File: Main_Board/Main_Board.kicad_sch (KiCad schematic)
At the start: 0 parts

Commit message: PCB init
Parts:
- added H1, H2: MountingHole_Pad, MountingHole:MountingHole_3.2mm_M3_DIN965_Pad_TopBottom, symbol Mechanical:MountingHole_Pad
- added H3, H4: MountingHole_Pad, MountingHole:MountingHole_2.2mm_M2, symbol Mechanical:MountingHole_Pad
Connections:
- new net GND: H1.1, H2.1, H3.1, H4.1

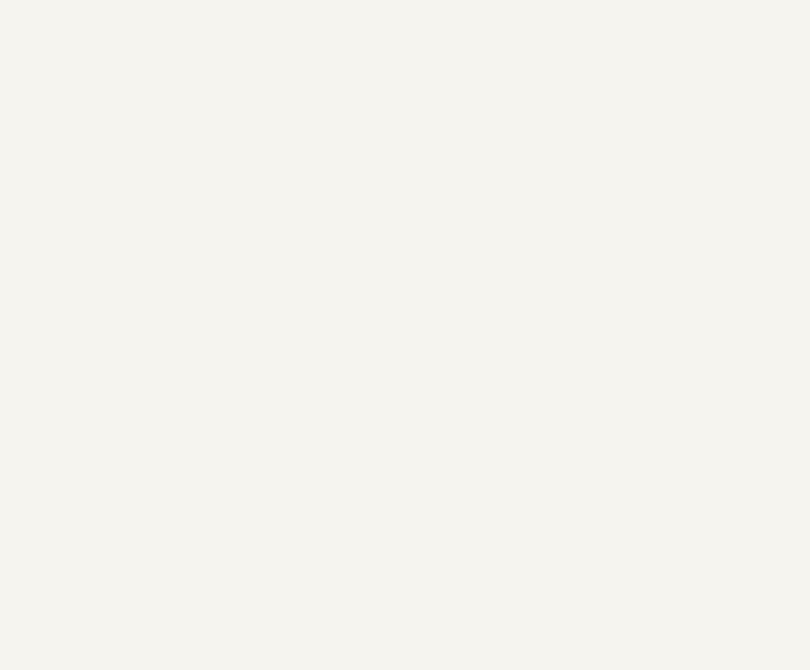
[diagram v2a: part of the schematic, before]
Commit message: Add pyro channels x2
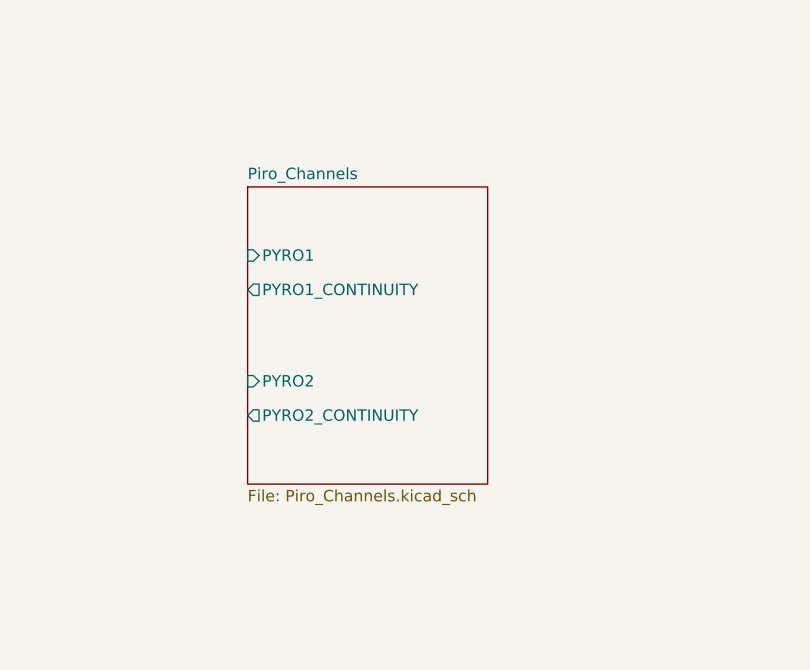
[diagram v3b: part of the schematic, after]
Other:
- added sheet Piro_Channels (Piro_Channels.kicad_sch)
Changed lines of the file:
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@@
 		(dnp no)
 		(fields_autoplaced yes)
-		(property "Reference" "#PWR096"
+		(property "Reference" "#PWR04"
 			(at 58.42 38.1 0)
 			(hide yes)
@@
 			(project "Main_Board"
 				(path "/7481738f-7c20-40bb-99b0-6ccd4168db33"
-					(reference "#PWR096")
+					(reference "#PWR04")
 					(unit 1)
 				)
@@
 		(dnp no)
 		(fields_autoplaced yes)
-		(property "Reference" "#PWR093"
+		(property "Reference" "#PWR01"
 			(at 31.75 38.1 0)
 			(hide yes)
@@
 			(project "Main_Board"
 				(path "/7481738f-7c20-40bb-99b0-6ccd4168db33"
-					(reference "#PWR093")
+					(reference "#PWR01")
 					(unit 1)
 				)
@@
 		(dnp no)
 		(fields_autoplaced yes)
-		(property "Reference" "#PWR094"
+		(property "Reference" "#PWR02"
 			(at 40.64 38.1 0)
 			(hide yes)
@@
 			(project "Main_Board"
 				(path "/7481738f-7c20-40bb-99b0-6ccd4168db33"
-					(reference "#PWR094")
+					(reference "#PWR02")
 					(unit 1)
 				)
@@
 		(dnp no)
 		(fields_autoplaced yes)
-		(property "Reference" "#PWR095"
+		(property "Reference" "#PWR03"
 			(at 49.53 38.1 0)
 			(hide yes)
@@
 			(project "Main_Board"
 				(path "/7481738f-7c20-40bb-99b0-6ccd4168db33"
-					(reference "#PWR095")
+					(reference "#PWR03")
 					(unit 1)
 				)
@@
 				)
 			)
+		)
+	)
+	(sheet
+		(at 93.98 78.74)
+		(size 26.67 33.02)
+		(exclude_from_sim no)
+		(in_bom yes)
+		(on_board yes)
+		(dnp no)
+		(fields_autoplaced yes)
+		(stroke
+			(width 0.1524)
+			(type solid)
+		)
+		(fill
+			(color 0 0 0 0)
+		)
+		(property "Sheetname" "Piro_Channels"
+			(at 93.98 78.0284 0)
+			(show_name no)
+			(do_not_autoplace no)
+			(effects
+				(font
+					(size 1.27 1.27)
+				)
+				(justify left bottom)
+			)
+		)
+		(property "Sheetfile" "Piro_Channels.kicad_sch"
+			(at 93.98 112.3446 0)
+			(show_name no)
+			(do_not_autoplace no)
+			(effects
+				(font
+					(size 1.27 1.27)
+				)
+				(justify left top)
+			)
+		)
+		(pin "PYRO2_CONTINUITY" output
+			(at 93.98 104.14 180)
+			(effects
+				(font
+					(size 1.27 1.27)
+				)
+				(justify left)
+			)
+		)
+		(pin "PYRO2" input
+			(at 93.98 100.33 180)
+			(effects
+				(font
+					(size 1.27 1.27)
+				)
+				(justify left)
+			)
+		)
+		(pin "PYRO1_CONTINUITY" output
+			(at 93.98 90.17 180)
+			(effects
+				(font
+					(size 1.27 1.27)
+				)
+				(justify left)
+			)
+		)
+		(pin "PYRO1" input
+			(at 93.98 86.36 180)
+			(effects
+				(font
+					(size 1.27 1.27)
+				)
+				(justify left)
+			)
+		)
+		(instances
+			(project "Main_Board"
+				(path "/7481738f-7c20-40bb-99b0-6ccd4168db33"
+					(page "10")
+				)
+			)

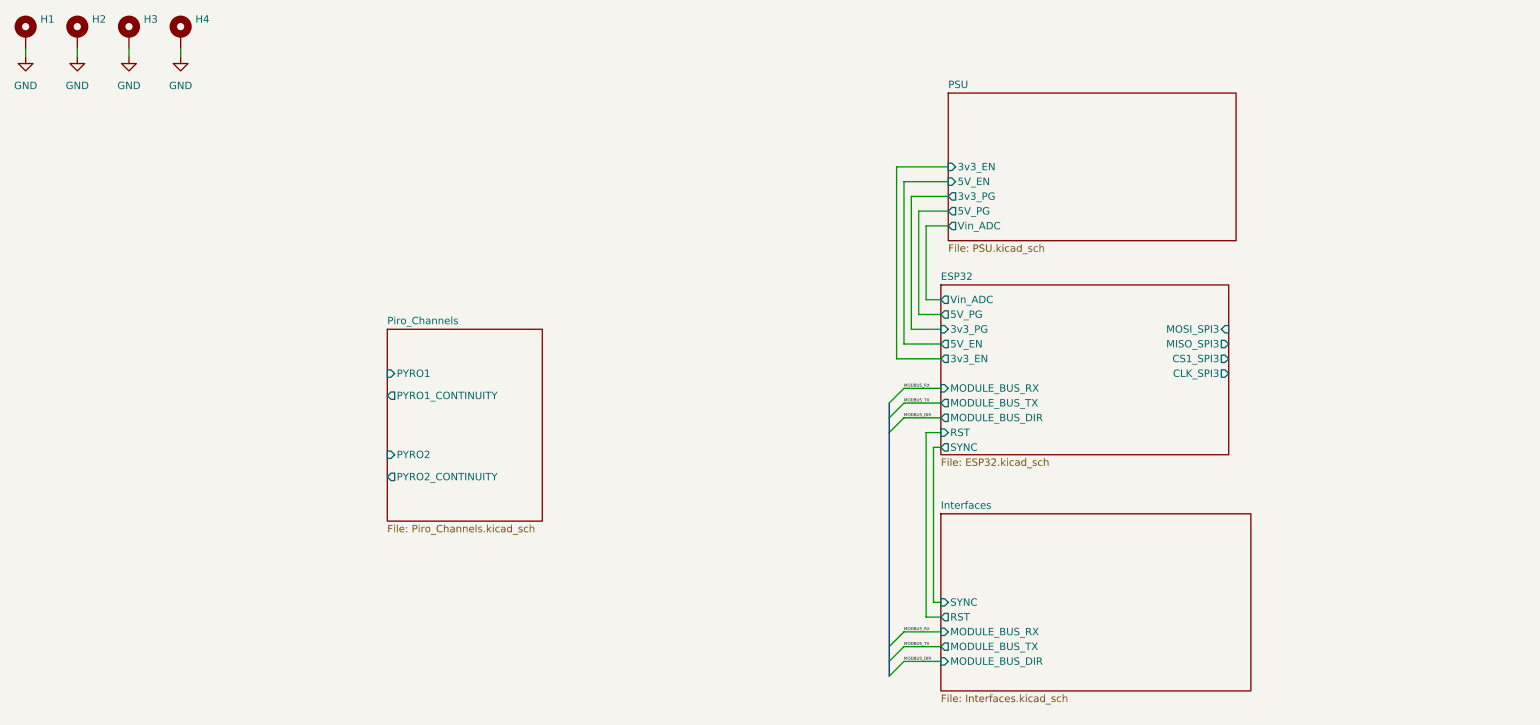
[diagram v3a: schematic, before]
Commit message: Module bus fix
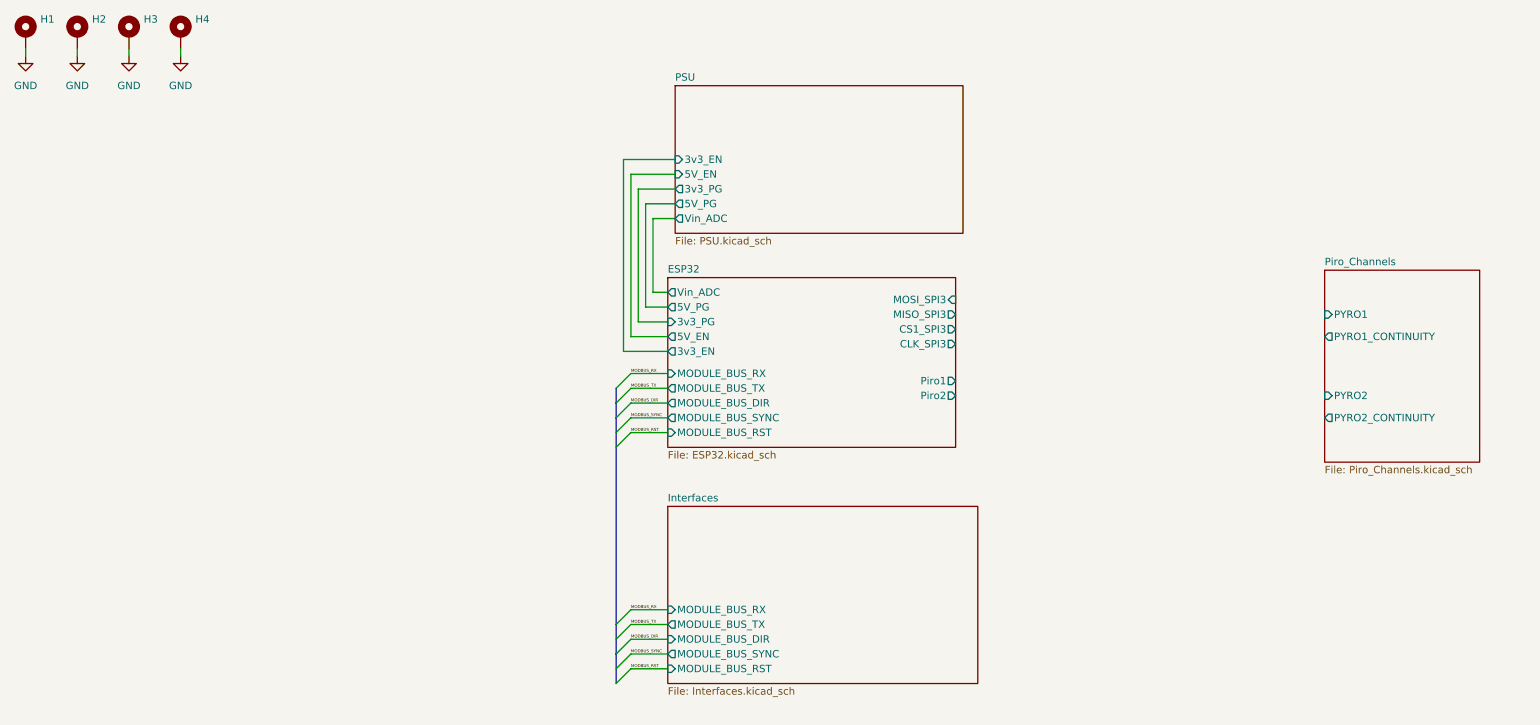
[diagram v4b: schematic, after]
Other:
- sheet ESP32 ports: added MODULE_BUS_RST, MODULE_BUS_SYNC, Piro1, Piro2; removed RST, SYNC
- sheet Interfaces ports: added MODULE_BUS_RST, MODULE_BUS_SYNC; removed RST, SYNC

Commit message: Update main sheet for pyros
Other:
- sheet ESP32 ports: added PYRO1, PYRO1_CONTINUITY, PYRO2, PYRO2_CONTINUITY; removed Piro1, Piro2
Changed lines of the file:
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@@
+	(wire
+		(pts
+			(xy 191.77 92.71) (xy 207.01 92.71)
+		)
+		(stroke
+			(width 0)
+			(type default)
+		)
+	)
 	(wire
 		(pts
@@
 	(wire
 		(pts
+			(xy 191.77 87.63) (xy 207.01 87.63)
+		)
+		(stroke
+			(width 0)
+			(type default)
+		)
+	)
+	(wire
+		(pts
 			(xy 135.89 52.07) (xy 135.89 80.01)
 		)
@@
 	(wire
 		(pts
+			(xy 191.77 90.17) (xy 207.01 90.17)
+		)
+		(stroke
+			(width 0)
+			(type default)
+		)
+	)
+	(wire
+		(pts
 			(xy 142.24 74.93) (xy 138.43 74.93)
 		)
@@
 		(pts
 			(xy 133.35 91.44) (xy 133.35 93.98)
+		)
+		(stroke
+			(width 0)
+			(type default)
+		)
+	)
+	(wire
+		(pts
+			(xy 191.77 95.25) (xy 207.01 95.25)
 		)
 		(stroke
@@
 	)
 	(sheet
-		(at 255.27 68.58)
-		(size 26.67 33.02)
+		(at 207.01 83.82)
+		(size 26.67 15.24)
 		(exclude_from_sim no)
 		(in_bom yes)
@@
 		)
 		(property "Sheetname" "Piro_Channels"
-			(at 255.27 67.8684 0)
+			(at 207.01 83.1084 0)
 			(show_name no)
 			(do_not_autoplace no)
@@
 		)
 		(property "Sheetfile" "Piro_Channels.kicad_sch"
-			(at 255.27 102.1846 0)
+			(at 207.01 99.6446 0)
 			(show_name no)
 			(do_not_autoplace no)
@@
 		)
 		(pin "PYRO2_CONTINUITY" output
-			(at 255.27 93.98 180)
+			(at 207.01 95.25 180)
 			(effects
 				(font
@@
 		)
 		(pin "PYRO2" input
-			(at 255.27 90.17 180)
+			(at 207.01 90.17 180)
 			(effects
 				(font
@@
 		)
 		(pin "PYRO1_CONTINUITY" output
-			(at 255.27 80.01 180)
+			(at 207.01 92.71 180)
 			(effects
 				(font
@@
 		)
 		(pin "PYRO1" input
-			(at 255.27 76.2 180)
+			(at 207.01 87.63 180)
 			(effects
 				(font
@@
 			)
 		)
-		(pin "Piro1" output
+		(pin "PYRO1" output
 			(at 191.77 87.63 0)
 			(effects
@@
 			)
 		)
-		(pin "Piro2" output
+		(pin "PYRO2" output
 			(at 191.77 90.17 0)
 			(effects
 				(font
+					(size 1.27 1.27)
+				)
+				(justify right)
+			)
+		)
+		(pin "PYRO1_CONTINUITY" input
+			(at 191.77 92.71 0)
+			(effects
+				(font
+					(size 1.27 1.27)
+				)
+				(justify right)
+			)
+		)
+		(pin "PYRO2_CONTINUITY" input
+			(at 191.77 95.25 0)
+			(effects
+				(font

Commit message: Pyro layout + schematic fix
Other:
- sheet Piro_Channels renamed Pyro_Channels (page 10)
- sheet Pyro_Channels (page 10) ports: added PYRO1_INPUT, PYRO2_INPUT; removed PYRO1, PYRO2
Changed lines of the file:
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@@
 			(color 0 0 0 0)
 		)
-		(property "Sheetname" "Piro_Channels"
+		(property "Sheetname" "Pyro_Channels (page 10)"
 			(at 176.53 100.8884 0)
 			(show_name no)
@@
 			)
 		)
-		(pin "PYRO2_CONTINUITY" output
-			(at 176.53 113.03 180)
+		(pin "PYRO1_INPUT" input
+			(at 176.53 105.41 180)
 			(effects
 				(font
@@
 			)
 		)
-		(pin "PYRO2" input
+		(pin "PYRO2_INPUT" input
 			(at 176.53 107.95 180)
+			(effects
+				(font
+					(size 1.27 1.27)
+				)
+				(justify left)
+			)
+		)
+		(pin "PYRO2_CONTINUITY" output
+			(at 176.53 113.03 180)
 			(effects
 				(font
@@
 			(effects
 				(font
-					(size 1.27 1.27)
-				)
-				(justify left)
-			)
-		)
-		(pin "PYRO1" input
-			(at 176.53 105.41 180)
-			(effects
-				(font

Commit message: nettie add /gnd split
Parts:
- added NT1: NetTie_2, NetTie:NetTie-2_SMD_Pad2.0mm, symbol Device:NetTie_2
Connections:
- net GND: now also NT1.1
- new net GNDPWR: NT1.2
